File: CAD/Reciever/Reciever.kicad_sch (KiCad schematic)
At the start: 45 parts, among them J1 Conn_01x02, J2 Output

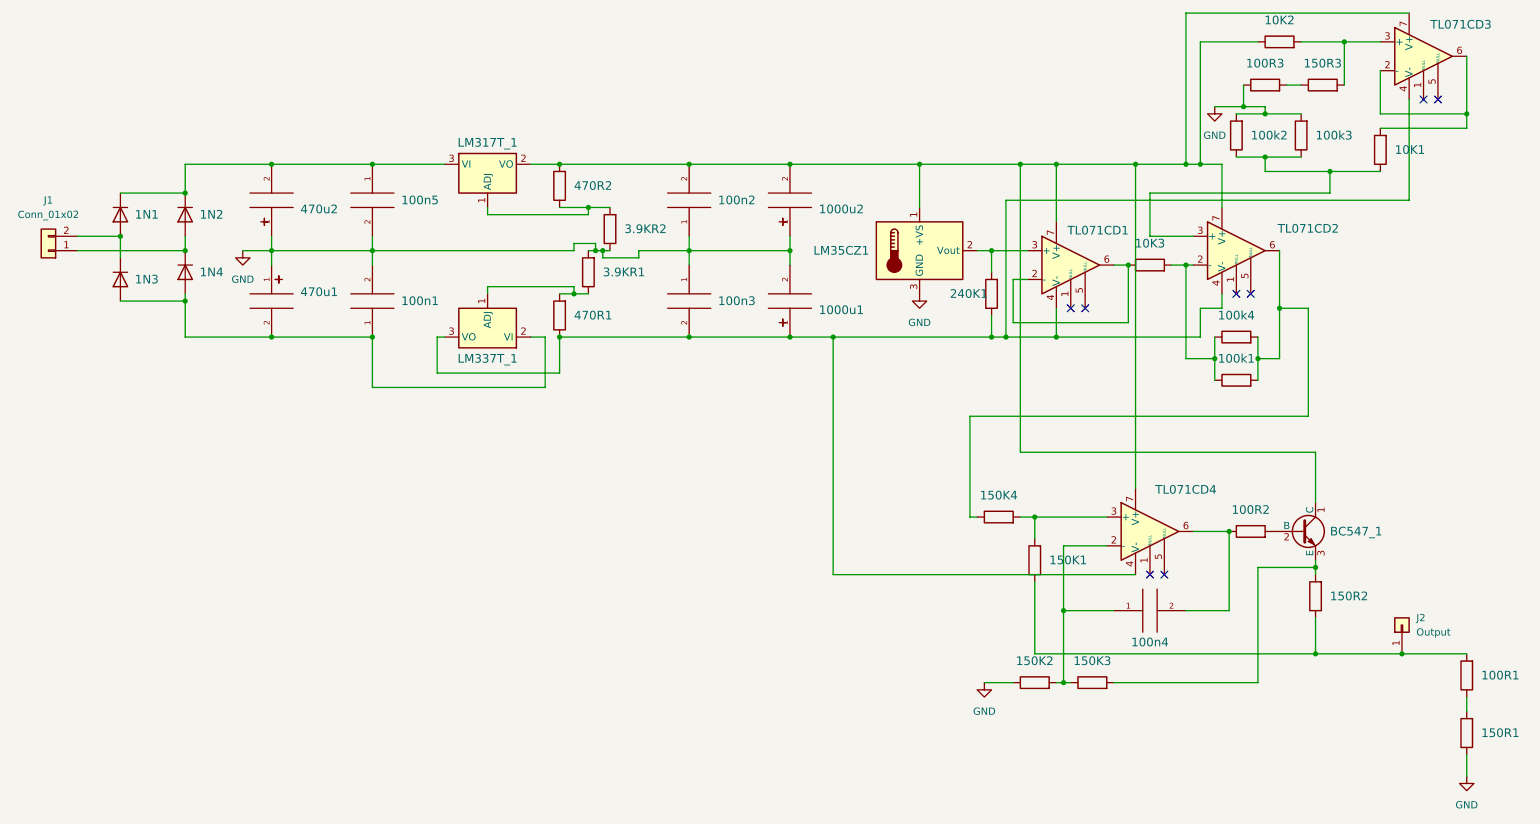
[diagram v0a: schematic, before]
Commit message: General cleanup, Reciever circuit CAD made
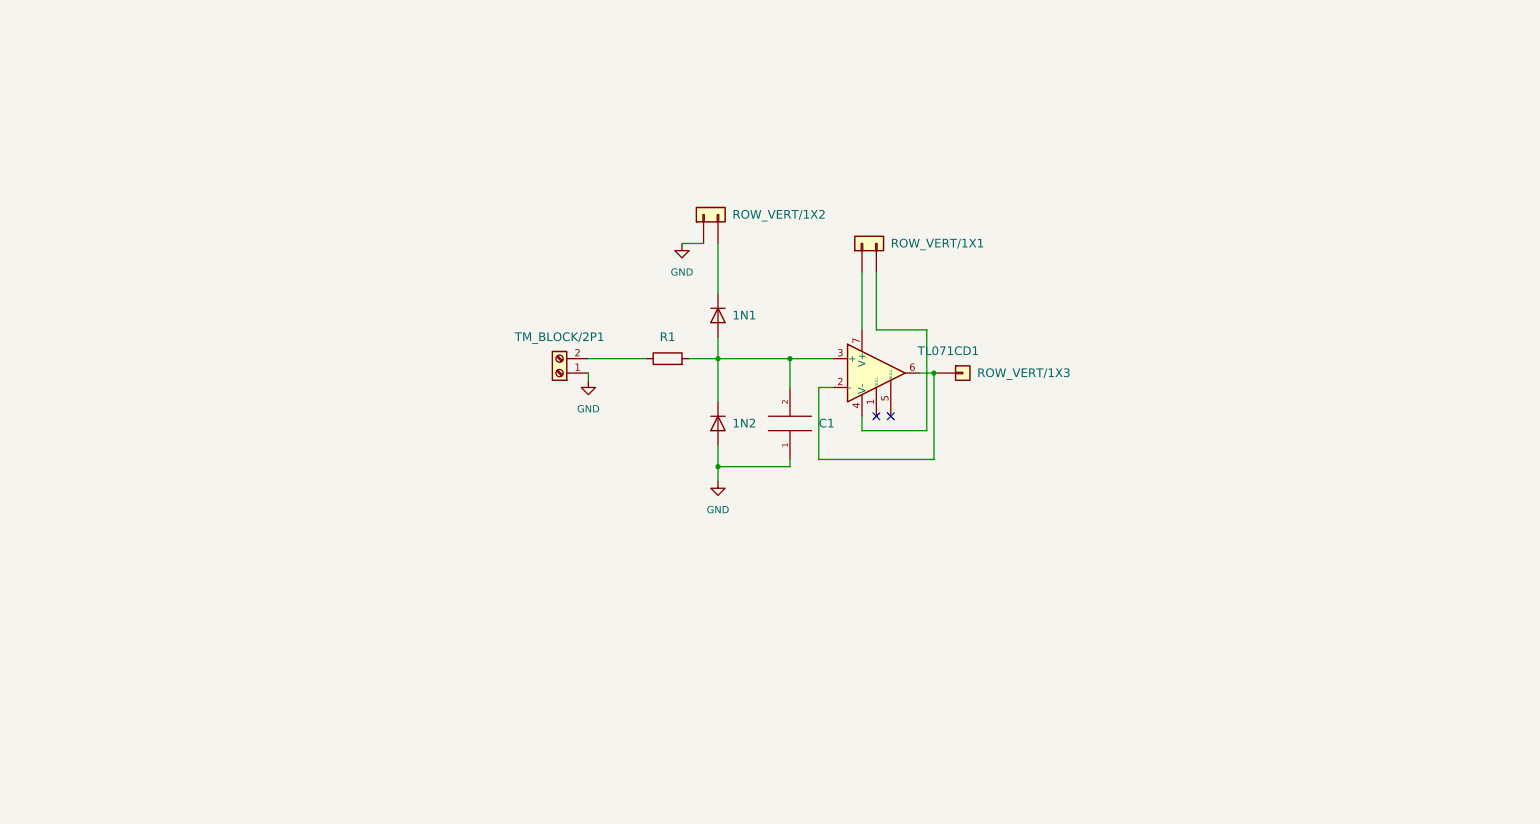
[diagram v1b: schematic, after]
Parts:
- removed 1000u1, 1000u2: 1000UF_50V_ELE, VAMK_C:C_P_5_0_13, symbol VAMK_C:1000UF_50V_ELE
- removed 100R1, 100R2, 100R3: 100R, VAMK_R_SMD:1206, symbol VAMK_R_SMD:100R
- removed 100k1, 100k2, 100k3, 100k4: 100k, VAMK_R_SMD:1206, symbol VAMK_R_SMD:100k
- removed 100n1, 100n2, 100n3, 100n4, 100n5: 100NF_50V_CER, VAMK_C_SMD:C1206, symbol VAMK_C_SMD:100NF_50V_CER
- removed 10K1, 10K2, 10K3: 10k, VAMK_R_SMD:1206, symbol VAMK_R_SMD:10k
- removed 150K1, 150K2, 150K3, 150K4: 150k, VAMK_R_SMD:1206, symbol VAMK_R_SMD:150k
- removed 150R1, 150R2, 150R3: 150R, VAMK_R_SMD:1206, symbol VAMK_R_SMD:150R
- removed 1N1, 1N2, 1N3, 1N4: 1N4007, VAMK_D:DO41, symbol VAMK_D:1N4007
- removed 240K1: 240k, VAMK_R:R3_5W, symbol VAMK_R:240k
- removed 3.9KR1, 3.9KR2: 3.9k, VAMK_R_SMD:1206, symbol VAMK_R_SMD:3.9k
- removed 470R1, 470R2: 470R, VAMK_R_SMD:1206, symbol VAMK_R_SMD:470R
- removed 470u1, 470u2: 470UF_50V_ELE, VAMK_C:C_P_5_0_13, symbol VAMK_C:470UF_50V_ELE
- removed BC547_1: BC547_TO92_0.1A, VAMK_ANA:TO-92, symbol VAMK_ANA:BC547_TO92_0.1A
- removed J1: Conn_01x02, Connector_JST:JST_NV_B02P-NV_1x02_P5.00mm_Vertical, symbol Connector_Generic:Conn_01x02
- removed J2: Output, Connector_PinHeader_1.27mm:PinHeader_1x01_P1.27mm_Vertical, symbol Connector_Generic:Conn_01x01
- removed LM317T_1: LM317T_TO220_1.5A, VAMK_ANA:TO-220, symbol VAMK_ANA:LM317T_TO220_1.5A
- removed LM337T_1: LM337T_TO220_1.5A, VAMK_ANA:TO-220, symbol VAMK_ANA:LM337T_TO220_1.5A
- removed LM35CZ1: LM35CZ_TO92, VAMK_IC:TO-92, symbol VAMK_IC:LM35CZ_TO92
- removed TL071CD2, TL071CD3, TL071CD4: TL071CD_SO8, VAMK_IC_SMD:SO8IC, symbol VAMK_IC_SMD:TL071CD_SO8
- added 1N1, 1N2: 1N4148, VAMK_D:DO41, symbol VAMK_D:1N4148
- added C1: 10NF_50V_CER, VAMK_C_SMD:C1206, symbol VAMK_C_SMD:10NF_50V_CER
- added R1: 100R, VAMK_R_SMD:1206, symbol VAMK_R_SMD:100R
- added ROW_VERT/1X1, ROW_VERT/1X2: ROW_VERT_1X2, VAMK_CON:ROW_VERT_1x2, symbol VAMK_CON:ROW_VERT_1X2
- added ROW_VERT/1X3: ROW_VERT_1X1, VAMK_CON:ROW_VERT_1x1, symbol VAMK_CON:ROW_VERT_1X1
- added TM_BLOCK/2P1: TM_BLOCK_2P, VAMK_CON:TM_BLOCK_2P, symbol VAMK_CON:TM_BLOCK_2P
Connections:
- net GND: now also 1N2.2 (A), C1.1, ROW_VERT/1X2.1 (Pin_1), TM_BLOCK/2P1.1 (Pin_1)
- net at TL071CD1.4 (V-): now also ROW_VERT/1X1.2 (Pin_2)
- net at TL071CD1.7 (V+): now also ROW_VERT/1X1.1 (Pin_1)
- net at TL071CD1.3 (+): now also 1N1.2 (A), 1N2.1 (K), C1.2, R1.2
- net at TL071CD1.2 (-), TL071CD1.6: now also ROW_VERT/1X3.1 (Pin_1)
- new net: R1.1, TM_BLOCK/2P1.2 (Pin_2)
- new net: 1N1.1 (K), ROW_VERT/1X2.2 (Pin_2)
- no-connect marks 8 -> 2
